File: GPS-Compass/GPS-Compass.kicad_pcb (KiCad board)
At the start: 4 copper layers, 100 x 78.5 mm, 115 parts, among them IC1 TPS565242DRLR, J1 FFC2B28-12-G, J2 Motor_conn, J3 FFC2B28-12-G, J4 01x10, J5 USB_TypeC, Q1 Q_PMOS, Q2 Q_PMOS, SW1 RESET, SW2 BOOT, U1 DRV8834RGER, U2 AP62300Z6, U3 USBLC6-2SC6, U4 ESP32-S3-WROOM-1, U5 BQ25887

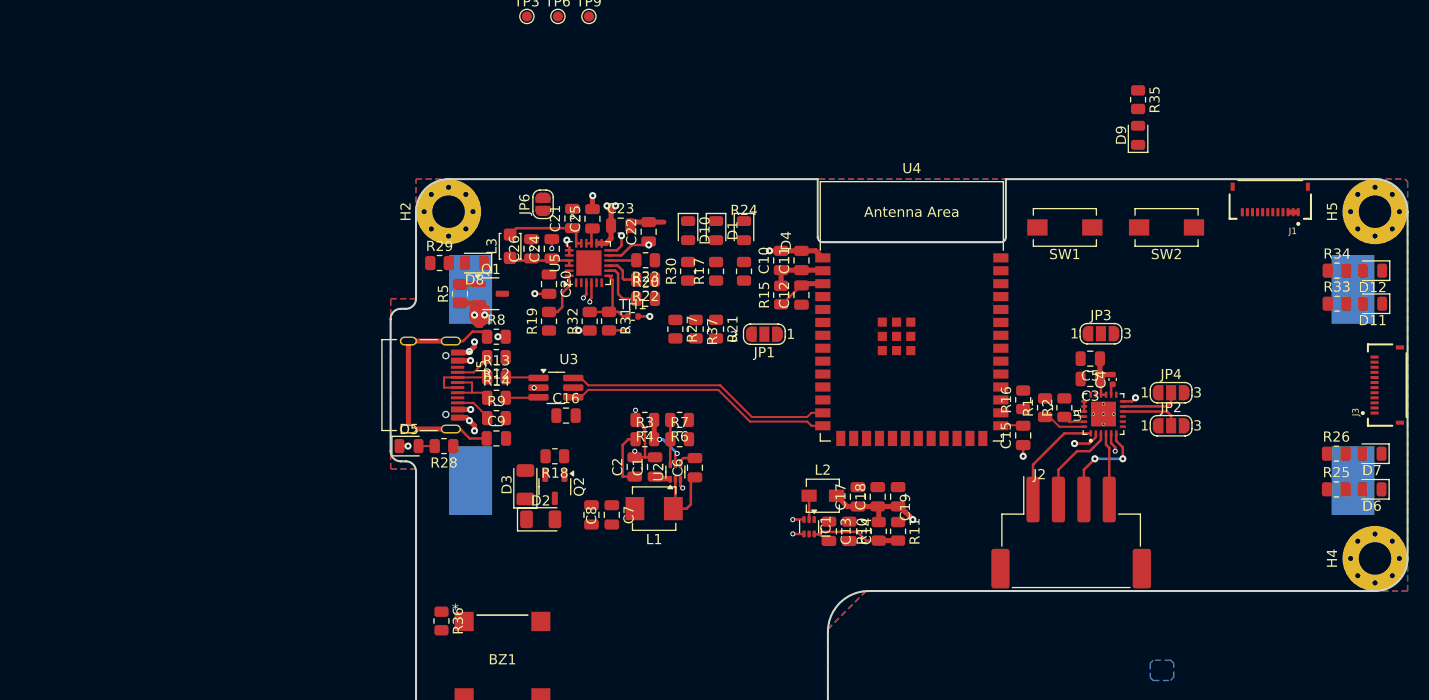
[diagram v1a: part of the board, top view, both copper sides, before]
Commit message: new usb charger
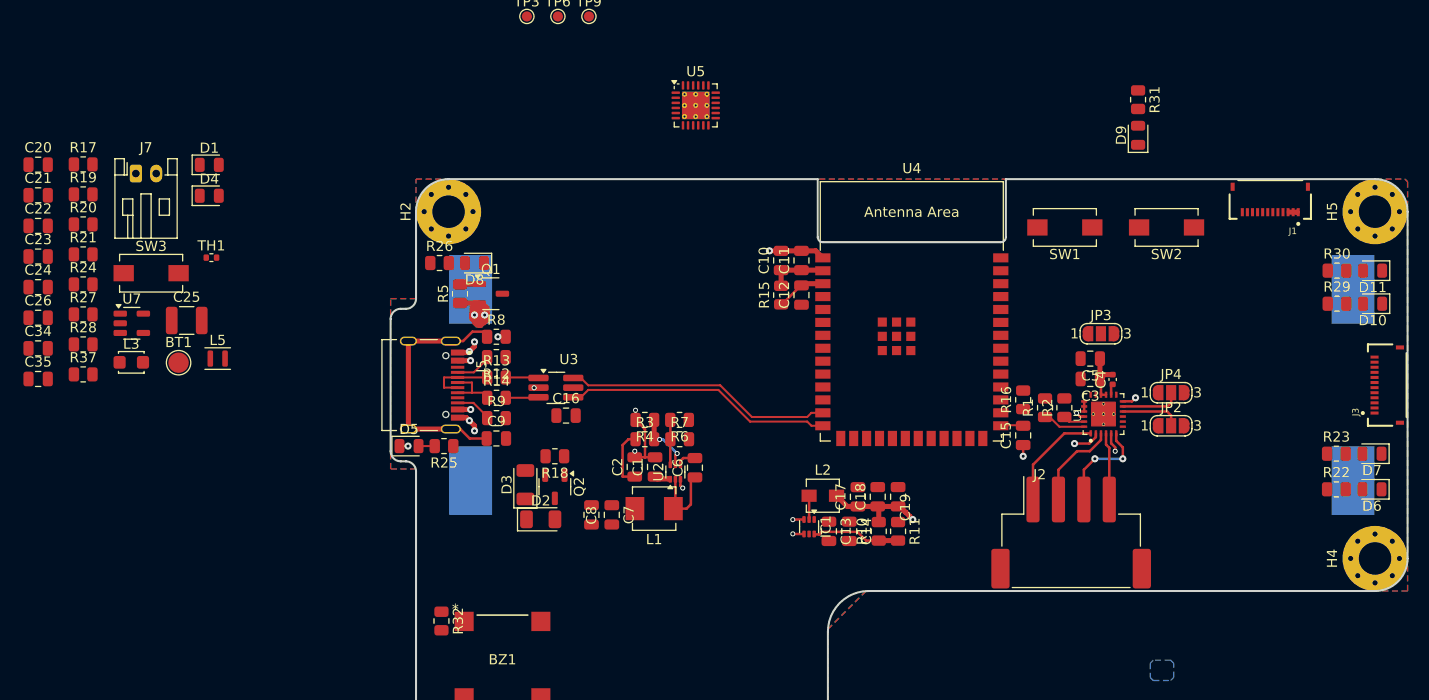
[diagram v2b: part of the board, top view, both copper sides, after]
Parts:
- removed the D10 at (100.8, 48.1)
- removed JP1: Jumper, Jumper:SolderJumper-3_P1.3mm_Open_RoundedPad1.0x1.5mm_NumberLabels
- removed JP6: Jumper, Jumper:SolderJumper-2_P1.3mm_Open_RoundedPad1.0x1.5mm
- removed the R22 at (96.6, 52.9)
- removed the R23 at (96.6, 51.0)
- removed the R30 at (100.8, 52.1)
- removed the R31 at (93.0, 57.0)
- removed the R32 at (91.1, 57.0)
- added BT1: LiPo cell, TestPoint:TestPoint_Pad_D2.0mm, F.Cu at (50.6, 61.0)
- added C34: 22u, Capacitor_SMD:C_0805_2012Metric, F.Cu at (36.8, 59.6)
- added C35: 100n, Capacitor_SMD:C_0805_2012Metric, F.Cu at (36.8, 62.6)
- added J7: Conn_01x02_Pin, Connector_JST:JST_PH_S2B-PH-K_1x02_P2.00mm_Horizontal, F.Cu at (46.5, 42.5)
- added L5: 2,2u, Inductor_SMD:L_Murata_DFE201610P, F.Cu at (54.5, 60.6)
- added R28: 30.1k, Resistor_SMD:R_0805_2012Metric, F.Cu at (41.3, 59.2)
- added SW3: SHIP-MODE, gps-compass_brd:SW_SPST_EVQPE1, F.Cu at (48.0, 52.2)
- added U7: TPS613222ADBV, Package_TO_SOT_SMD:SOT-23-5, F.Cu at (46.0, 57.2)
- C22: value 4.7u -> 10u
- C23: value 10u -> 4.7u
- C24: value 100n -> 10u
- C25: value 44u -> 47u; footprint Capacitor_SMD:C_0805_2012Metric -> Capacitor_SMD:C_1210_3225Metric
- L3: value 1u -> 2.2uH
- R20: value 383R -> RLIM
- R21: value 10k -> 2.2k
- R24: value 2.2k -> 10k
- R27: value 10k -> 5.23k
- U5: value BQ25887 -> BQ25895RTW; footprint Package_DFN_QFN:VQFN-24-1EP_4x4mm_P0.5mm_EP2.5x2.5mm -> Package_DFN_QFN:Texas_RTW_WQFN-24-1EP_4x4mm_P0.5mm_EP2.7x2.7mm_ThermalVias
- moved R24 65.0 mm to (41.3, 53.4), turned to 0 degrees
- moved R17 63.1 mm to (41.3, 41.5), turned to 0 degrees
- moved R21 62.7 mm to (41.3, 50.4), turned to 0 degrees
- moved R37 60.4 mm to (41.3, 62.2), turned to 0 degrees
- moved C22 60.0 mm to (36.8, 47.6), turned to 0 degrees
- moved R27 58.2 mm to (41.3, 56.3), turned to 0 degrees
- moved C23 57.4 mm to (36.8, 50.6)
- moved R20 55.8 mm to (41.3, 47.5)
- moved D4 52.7 mm to (53.7, 44.6), turned to 0 degrees
- moved C21 52.6 mm to (36.8, 44.6), turned to 0 degrees
- moved C20 51.6 mm to (36.8, 41.6), turned to 0 degrees
- moved C24 50.7 mm to (36.8, 53.6), turned to 0 degrees
- moved D1 50.2 mm to (53.7, 41.6), turned to 0 degrees
- moved C26 49.0 mm to (36.8, 56.6), turned to 0 degrees
- moved R19 47.5 mm to (41.3, 44.5), turned to 0 degrees
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- renumbered D11 to D10, D12 to D11, R25 to R22, R26 to R23, R28 to R25, R29 to R26, R33 to R29, R34 to R30, R35 to R31, R36 to R32
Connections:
- C13 pad 1: +5V -> VIN
- C14 pad 1: +5V -> VIN
- C21 pad 1: /SWC -> Net-(C21-Pad1)
- C22 pad 1: /LDO -> VBATT
- C23 pad 1: VBATT -> REGN
- C24 pad 1: Net-(C24-Pad1) -> VSYS
- C25 pad 1: Net-(JP6-A) -> VOTG
- C26 pad 1: Net-(C24-Pad1) -> VSYS
- D4 pad 1: /~{INT} -> /DSEL
- IC1 pad 1: +5V -> VIN
- IC1 pad 5: +5V -> VIN
- L3 pad 1: Net-(C24-Pad1) -> Net-(C21-Pad1)
- L3 pad 2: /SWC -> VSYS
- Q1 pad 2: VBATT -> VSYS
- Q1 pad 3: +8V -> VIN
- R19 pad 1: +3V3 -> /STAT
- R19 pad 2: /PSEL -> +3V3
- R21 pad 1: /STAT -> +3V3
- R21 pad 2: +3V3 -> Net-(D4-A)
- R24 pad 1: +3V3 -> /DSEL
- R24 pad 2: Net-(D4-A) -> +3V3
- R27 pad 1: /~{INT} -> /TS
- R27 pad 2: +3V3 -> REGN
- R37 pad 1: /~{PG} -> +3V3
- R37 pad 2: +3V3 -> /INT
- R5 pad 1: VBATT -> VSYS
- U5 pad 1: /~{PG} -> USB_VBUS
- U5 pad 10: Net-(U5-CBSET) -> Net-(U5-ILIM)
- U5 pad 11: /LDO -> /TS
- U5 pad 12: Net-(U5-BTST) -> Net-(U5-~{QON})
- U5 pad 15: Net-(JP6-A) -> VSYS
- U5 pad 16: Net-(JP6-A) -> VSYS
- U5 pad 17: /SWC -> GND
- U5 pad 18: /SWC -> GND
- U5 pad 19: GND -> Net-(C21-Pad1)
- U5 pad 2: /STAT -> /D+
- U5 pad 20: GND -> Net-(C21-Pad1)
- U5 pad 21: Net-(C24-Pad1) -> Net-(U5-BTST)
- U5 pad 22: Net-(C24-Pad1) -> REGN
- U5 pad 23: USB_VBUS -> VOTG
- U5 pad 24: /PSEL -> /DSEL
- U5 pad 25: (no net) -> GND
- U5 pad 3: GND -> /D-
- U5 pad 4: /SDA -> /STAT
- U5 pad 6: /~{INT} -> /SDA
- U5 pad 7: /TS -> /INT
- U5 pad 8: Net-(U5-ILIM) -> /OTG
- U5 pad 9: Net-(U5-MID) -> /~{CE}
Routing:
- net GND: track 42.6 -> 28.9 mm, vias 24 -> 16
- net /SWC: track 8.53 -> 0.00 mm
- net /TS: track 7.94 -> 0.00 mm
- net VBATT: track 13.5 -> 6.60 mm, vias 4 -> 2
- net /LDO: track 6.57 -> 0.00 mm, vias 2 -> 0
- net Net-(C24-Pad1): track 6.39 -> 0.00 mm
- net Net-(U5-ILIM): track 5.05 -> 0.00 mm
- net /PSEL: track 4.86 -> 0.00 mm
- net Net-(U5-MID): track 3.73 -> 0.00 mm
- net Net-(U5-BTST): track 3.22 -> 0.00 mm, vias 2 -> 0
- net Net-(U5-CBSET): track 2.74 -> 0.00 mm
- net Net-(JP6-A): track 2.00 -> 0.00 mm
- net /SDA: track 7.71 -> 5.76 mm, vias 1 -> 0

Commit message: UI changes
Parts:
- removed C25: 47u, Capacitor_SMD:C_1210_3225Metric
- removed C26: 10u, Capacitor_SMD:C_0805_2012Metric
- removed C34: 22u, Capacitor_SMD:C_0805_2012Metric
- removed C35: 100n, Capacitor_SMD:C_0805_2012Metric
- removed D1: LED, LED_SMD:LED_0805_2012Metric
- removed the D9 at (145.0, 38.7)
- removed L5: 2,2u, Inductor_SMD:L_Murata_DFE201610P
- removed the R17 at (41.3, 41.5)
- removed the R28 at (41.3, 59.2)
- removed the R31 at (145.0, 35.2)
- removed R37: 10k, Resistor_SMD:R_0805_2012Metric
- removed SW3: SHIP-MODE, gps-compass_brd:SW_SPST_EVQPE1
- removed U7: TPS613222ADBV, Package_TO_SOT_SMD:SOT-23-5
- added C1: 100n, Capacitor_SMD:C_0805_2012Metric, F.Cu at (44.9, 45.9)
- added C17: 100n, Capacitor_SMD:C_0805_2012Metric, F.Cu at (44.9, 51.9)
- added C18: 1u, Capacitor_SMD:C_0805_2012Metric, F.Cu at (49.3, 45.9)
- added C19: 47n, Capacitor_SMD:C_0805_2012Metric, F.Cu at (49.3, 48.9)
- added C4: 22u, Capacitor_SMD:C_0805_2012Metric, F.Cu at (44.9, 48.9)
- added D5: LED, LED_SMD:LED_0805_2012Metric, F.Cu at (54.1, 61.2)
- added D6: LED, LED_SMD:LED_0805_2012Metric, F.Cu at (54.1, 64.2)
- added J2: Conn_01x02_Pin, Connector_JST:JST_PH_S2B-PH-K_1x02_P2.00mm_Horizontal, F.Cu at (29.7, 46.8)
- added J8: Conn_01x02_Pin, Connector_Wire:SolderWire-0.1sqmm_1x02_P3.6mm_D0.4mm_OD1mm_Relief, F.Cu at (36.9, 46.5)
- added L1: 2,2u, Inductor_SMD:L_Murata_DFE201610P, F.Cu at (48.5, 64.2)
- added R11: 10k, Resistor_SMD:R_0805_2012Metric, F.Cu at (29.0, 40.0)
- added R14: 10k, Resistor_SMD:R_0805_2012Metric, F.Cu at (29.0, 42.9)
- added R22: 2.2k, Resistor_SMD:R_0805_2012Metric, F.Cu at (33.4, 42.9)
- added R23: 10k, Resistor_SMD:R_0805_2012Metric, F.Cu at (37.8, 34.1)
- added R25: 10k, Resistor_SMD:R_0805_2012Metric, F.Cu at (37.8, 40.0)
- added R26: RLIM, Resistor_SMD:R_0805_2012Metric, F.Cu at (37.8, 42.9)
- added R3: 10k, Resistor_SMD:R_0805_2012Metric, F.Cu at (29.0, 34.1)
- added R30: 10k, Resistor_SMD:R_0805_2012Metric, F.Cu at (42.2, 37.0)
- added R33: 5.23k, Resistor_SMD:R_0805_2012Metric, F.Cu at (42.2, 40.0)
- added R34: 30.1k, Resistor_SMD:R_0805_2012Metric, F.Cu at (42.2, 42.9)
- added R4: 2.2K, Resistor_SMD:R_0805_2012Metric, F.Cu at (29.0, 37.0)
- added SW4: SHIP-MODE, gps-compass_brd:SW_SPST_EVQPE1, F.Cu at (48.9, 35.1)
- added U2: TPS613222ADBV, Package_TO_SOT_SMD:SOT-23-5, F.Cu at (55.9, 35.0)
- C20: value 1u -> 10u
- C21: value 47n -> 4.7u
- C23: value 4.7u -> 47u; footprint Capacitor_SMD:C_0805_2012Metric -> Capacitor_SMD:C_1210_3225Metric
- J7: value Conn_01x02_Pin -> USB_TypeC; footprint Connector_JST:JST_PH_S2B-PH-K_1x02_P2.00mm_Horizontal -> sumec_brd:HRO_TYPE-C-31-M-12
- R19: value 10k -> 100k
- R20: value RLIM -> 2.2k
- R21: value 2.2k -> 36k
- R24: value 10k -> 36k
- R27: value 5.23k -> 2.2k
- moved U5 54.2 mm to (47.6, 40.8)
- moved TP1 53.1 mm to (44.2, 54.9)
- moved TP4 53.1 mm to (47.2, 54.9)
- moved TP7 53.1 mm to (50.3, 54.9)
- moved TP2 53.1 mm to (44.2, 58.0)
- moved TP3 53.1 mm to (44.2, 61.0)
- moved TP5 53.1 mm to (47.2, 58.0)
- moved TP6 53.1 mm to (47.2, 61.0)
- moved TP8 53.1 mm to (50.3, 58.0)
- moved TP9 53.1 mm to (50.3, 61.0)
- moved J7 22.8 mm to (32.8, 60.7)
- moved R27 22.3 mm to (42.2, 34.1)
- moved C23 19.9 mm to (53.5, 39.8)
- moved C24 17.0 mm to (53.8, 51.9)
- moved C21 17.0 mm to (53.8, 45.9)
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- renumbered C11 to C10, C17 to C11, C18 to C13, C19 to C14, C3 to C2, C4 to C3, C9 to C6, C13 to C7, C10 to C8, C14 to C9, D11 to D10, D5 to D2, D8 to D3, D6 to D7, D7 to D8, D10 to D9, J2 to J3, J3 to J4, J4 to J5, J5 to J6, JP2 to JP1, JP3 to JP2, JP4 to JP3, R12 to R10, R13 to R12, R14 to R13, R25 to R17, R26 to R18, R22 to R28, R23 to R29, R29 to R31, R30 to R32, R32 to R35, R8 to R6, R9 to R7, R10 to R8, R11 to R9
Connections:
- net /VM renamed VM
- net /VREFO renamed VREFO
- C20 pad 1: USB_VBUS -> VBATT
- C21 pad 1: Net-(C21-Pad1) -> REGN
- C21 pad 2: Net-(U5-BTST) -> GND
- C22 pad 1: VBATT -> VSYS
- C23 pad 1: REGN -> VOTG
- D2 pad 2: Net-(D5-A) -> Net-(D2-A)
- D4 pad 1: /DSEL -> GND
- L3 pad 1: Net-(C21-Pad1) -> Net-(C19-Pad1)
- R17 pad 2: Net-(D5-A) -> Net-(D2-A)
- R19 pad 1: /STAT -> Net-(C17-Pad1)
- R19 pad 2: +3V3 -> GND
- R20 pad 1: Net-(U5-ILIM) -> +3V3
- R20 pad 2: GND -> Net-(D4-A)
- R21 pad 1: +3V3 -> Net-(J7-CC2)
- R21 pad 2: Net-(D4-A) -> +3V3
- R24 pad 1: /DSEL -> Net-(J7-CC1)
- R27 pad 1: /TS -> +3V3
- R27 pad 2: REGN -> Net-(D6-A)
- U1 pad 13: /NFAULT -> Net-(U1-NFAULT)
- U4 pad 12: unconnected-(U4-IO8-Pad12) -> /SDA
- U4 pad 38: unconnected-(U4-IO2-Pad38) -> /STEP
- U4 pad 39: unconnected-(U4-IO1-Pad39) -> /INT
- U4 pad 4: unconnected-(U4-IO4-Pad4) -> /DIR
- U4 pad 7: unconnected-(U4-IO7-Pad7) -> /SCL
- U5 pad 19: Net-(C21-Pad1) -> Net-(C19-Pad1)
- U5 pad 20: Net-(C21-Pad1) -> Net-(C19-Pad1)
- U5 pad 9: /~{CE} -> GND
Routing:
- net Net-(D5-A): track 1.59 -> 0.00 mm
- net Net-(D2-A): track 0.00 -> 1.59 mm

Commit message: jkolsd
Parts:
- removed the BT1 at (44.7, 64.6)
- removed the C1 at (97.5, 71.3)
- removed the C1 at (44.9, 45.9)
- removed C17: 100n, Capacitor_SMD:C_0805_2012Metric
- removed C18: 1u, Capacitor_SMD:C_0805_2012Metric
- removed C19: 47n, Capacitor_SMD:C_0805_2012Metric
- removed C20, C22, C24: 10u, Capacitor_SMD:C_0805_2012Metric
- removed C21: 4.7u, Capacitor_SMD:C_0805_2012Metric
- removed C23: 47u, Capacitor_SMD:C_1210_3225Metric
- removed the C6 at (101.4, 71.4)
- removed the C7 at (93.2, 76.0)
- removed the C8 at (91.2, 76.0)
- removed D10, D4, D5, D6, D9: LED, LED_SMD:LED_0805_2012Metric
- removed J2: Conn_01x02_Pin, Connector_JST:JST_PH_S2B-PH-K_1x02_P2.00mm_Horizontal
- removed J7: USB_TypeC, sumec_brd:HRO_TYPE-C-31-M-12
- removed J8: Conn_01x02_Pin, Connector_Wire:SolderWire-0.1sqmm_1x02_P3.6mm_D0.4mm_OD1mm_Relief
- removed L1: 3.3u, Inductor_SMD:L_Vishay_IHLP-1616
- removed L1: 2,2u, Inductor_SMD:L_Murata_DFE201610P
- removed L3: 2.2uH, Inductor_SMD:L_Walsin_WLFM201609x
- removed Q2: Q_PMOS, Package_TO_SOT_SMD:SOT-23-3
- removed R14, R23, R25, R30: 10k, Resistor_SMD:R_0805_2012Metric
- removed the R18 at (87.7, 70.2)
- removed R19: 100k, Resistor_SMD:R_0805_2012Metric
- removed R20, R22, R27: 2.2k, Resistor_SMD:R_0805_2012Metric
- removed R21, R24: 36k, Resistor_SMD:R_0805_2012Metric
- removed R26: RLIM, Resistor_SMD:R_0805_2012Metric
- removed the R3 at (29.0, 34.1)
- removed the R3 at (96.5, 68.6)
- removed R31, R32: 220R, Resistor_SMD:R_0805_2012Metric
- removed R33: 5.23k, Resistor_SMD:R_0805_2012Metric
- removed R34: 30.1k, Resistor_SMD:R_0805_2012Metric
- removed the R4 at (96.5, 66.7)
- removed the R4 at (29.0, 37.0)
- removed TH1: 10k NTC, Resistor_SMD:R_0402_1005Metric
- removed TP1, TP2, TP3, TP4, TP5, TP6, TP7, TP8, TP9: TestPoint, TestPoint:TestPoint_Pad_D1.0mm
- removed U2: TPS613222ADBV, Package_TO_SOT_SMD:SOT-23-5
- removed U2: AP62300Z6, Package_TO_SOT_SMD:SOT-563
- removed U5: BQ25895RTW, Package_DFN_QFN:Texas_RTW_WQFN-24-1EP_4x4mm_P0.5mm_EP2.7x2.7mm_ThermalVias
- added C1: 100n, Capacitor_SMD:C_0805_2012Metric, F.Cu at (182.8, 100.5)
- added C3: 100nF, Capacitor_SMD:C_0805_2012Metric, F.Cu at (182.8, 78.4)
- added D1: LED, Connector_Wire:SolderWire-0.1sqmm_1x02_P3.6mm_D0.4mm_OD1mm_Relief, F.Cu at (186.0, 76.6)
- added H1: M3, MountingHole:MountingHole_3.2mm_M3, F.Cu at (187.0, 147.7)
- added H2: M3, MountingHole:MountingHole_3.2mm_M3, F.Cu at (187.0, 60.7)
- added J1: FFC2B28-12-G, gps-compass_brd:GCT_FFC2B28-12-G, F.Cu at (179.0, 63.2)
- added R1: 2.2k, Resistor_SMD:R_0805_2012Metric, F.Cu at (183.8, 130.2)
- added R10: 1k, Resistor_SMD:R_0805_2012Metric, F.Cu at (182.8, 109.9)
- added R2: 2.2k, Resistor_SMD:R_0805_2012Metric, F.Cu at (183.6, 71.0)
- added R3: 1k, Resistor_SMD:R_0805_2012Metric, F.Cu at (182.8, 102.5)
- added R4: 10k, Resistor_SMD:R_0805_2012Metric, F.Cu at (182.8, 104.5)
- added R5: 1k, Resistor_SMD:R_0805_2012Metric, F.Cu at (182.8, 87.8)
- added R8: 1k, Resistor_SMD:R_0805_2012Metric, F.Cu at (182.8, 80.4)
- added R9: 10k, Resistor_SMD:R_0805_2012Metric, F.Cu at (182.8, 82.4)
- added SW1: SPDT, Connector_Wire:SolderWire-0.1sqmm_1x02_P3.6mm_D0.4mm_OD1mm_Relief, F.Cu at (186.0, 142.9)
- added SW2: SW_SPDT, Connector_Wire:SolderWire-0.1sqmm_1x02_P3.6mm_D0.4mm_OD1mm_Relief, F.Cu at (186.0, 69.2)
- added SW3: EXT, Connector_Wire:SolderWire-0.1sqmm_1x02_P3.6mm_D0.4mm_OD1mm_Relief, F.Cu at (186.0, 106.1)
- added SW5: RESET, Connector_Wire:SolderWire-0.1sqmm_1x02_P3.6mm_D0.4mm_OD1mm_Relief, F.Cu at (186.0, 128.2)
- added SW6: EXT, Connector_Wire:SolderWire-0.1sqmm_1x02_P3.6mm_D0.4mm_OD1mm_Relief, F.Cu at (186.0, 91.3)
- added SW7: EXT, Connector_Wire:SolderWire-0.1sqmm_1x02_P3.6mm_D0.4mm_OD1mm_Relief, F.Cu at (186.0, 84.0)
- added SW8: EXT, Connector_Wire:SolderWire-0.1sqmm_1x02_P3.6mm_D0.4mm_OD1mm_Relief, F.Cu at (186.0, 113.4)
- C4: value 22u -> 100nF
- D2, D3: value D_Schottky -> LED; footprint Diode_SMD:D_1206_3216Metric -> Connector_Wire:SolderWire-0.1sqmm_1x02_P3.6mm_D0.4mm_OD1mm_Relief
- Q1: value Q_PMOS -> SI2393DS
- R6: value 52.3k -> 10k
- R7: value 10k -> 220R
- SW4: value SHIP-MODE -> RESET; footprint gps-compass_brd:SW_SPST_EVQPE1 -> Connector_Wire:SolderWire-0.1sqmm_1x02_P3.6mm_D0.4mm_OD1mm_Relief
- moved R11 169.8 mm to (182.8, 111.9)
- moved SW4 161.7 mm to (186.0, 120.8), turned to 90 degrees
- moved C4 150.0 mm to (182.8, 107.9), turned to 180 degrees
- moved D2 115.9 mm to (186.0, 135.5), turned to 90 degrees
- moved D3 104.4 mm to (186.0, 98.7)
- moved C2 88.5 mm to (182.8, 85.8), turned to 180 degrees
- moved R7 87.0 mm to (182.8, 95.1)
- moved R6 86.0 mm to (182.8, 89.8), turned to 0 degrees
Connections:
- C2 pad 1: +8V -> GND
- C2 pad 2: GND -> /DBNCD_2
- C4 pad 1: +5V -> GND
- C4 pad 2: GND -> /DBNCD_0
- D2 pad 1: +5V -> /MSW_ON
- D3 pad 1: +5V -> GND
- D3 pad 2: USB_VBUS -> Net-(D3-A)
- R11 pad 1: /SDA -> /DBNCD_0
- R6 pad 1: 5V_CONV -> /DBNCD_2
- R6 pad 2: Net-(U2-FB) -> +3V3
- R7 pad 1: Net-(U2-FB) -> /LED_EXT
- R7 pad 2: GND -> Net-(D3-A)
- SW4 pad 2: Net-(U5-~{QON}) -> /EN
- U4 pad 17: unconnected-(U4-IO9-Pad17) -> /MOSI
- U4 pad 5: unconnected-(U4-IO5-Pad5) -> /~{CS}
- U4 pad 6: unconnected-(U4-IO6-Pad6) -> /CLK
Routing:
- net /MSW_ON: track 1.90 -> 86.0 mm
- net +3V3: track 18.0 -> 93.2 mm, vias 3 -> 9
- net /GNSS_RST: track 0.00 -> 64.8 mm, vias 0 -> 1
- net /EN: track 4.94 -> 63.4 mm
- net /DBNCD_0: track 0.00 -> 52.1 mm, vias 0 -> 2
- net /DBNCD_1: track 0.00 -> 44.5 mm
- net /LED_EXT: track 0.00 -> 37.0 mm, vias 0 -> 2
- net /DBNCD_2: track 0.00 -> 31.1 mm
- net /DBNCD_3: track 0.00 -> 25.2 mm, vias 0 -> 2
- net /OTG_ON: track 0.00 -> 15.4 mm
- net Net-(U2-SW): track 7.43 -> 0.00 mm
- net +8V: track 7.25 -> 0.00 mm
- net Net-(U2-EN): track 5.90 -> 0.00 mm, vias 2 -> 0
- net Net-(U2-FB): track 4.49 -> 0.00 mm
- net Net-(D1-A): track 0.00 -> 2.88 mm
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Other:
- board size 100 x 78.5 mm -> 125.5 x 108.7 mm
- board text added: "DBNCD-0 GPIO"
- board text added: "DBNCD-1 GPIO"
- board text added: "DBNCD-2 GPIO"
- board text added: "DBNCD-3 GPIO"
- board text added: "EXTERNAL LED"
- board text added: "GNSS RESET"
- board text added: "MAIN SWITCH"
- board text added: "MCU RESET"
- board text added: "OTG ON"
- board text added: "OTG SWITCH"
- board text added: "POWER ON"
